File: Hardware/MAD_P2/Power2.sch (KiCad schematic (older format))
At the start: 91 parts, among them U13 XL1509-5.0, U14 XL1509-5.0, U15 AMS1117-3.3, U16 AMS1117-3.3, U18 AMS1117-3.3, U22 XL1509-5.0, U24 AMS1117-3.3

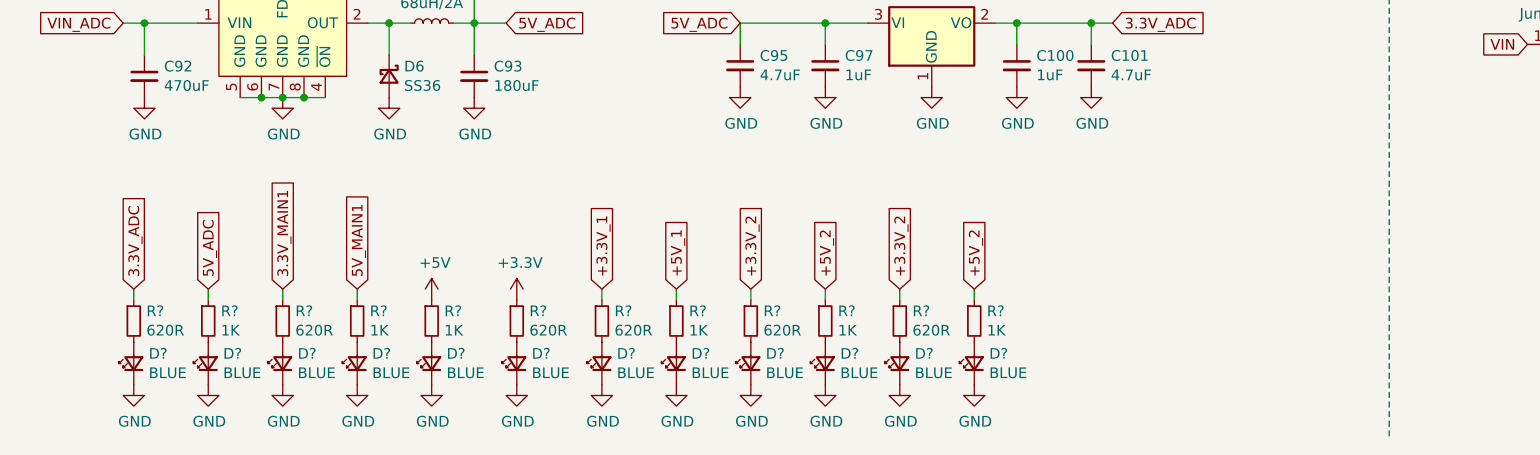
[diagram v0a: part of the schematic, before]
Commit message: added optional sd card socket for data
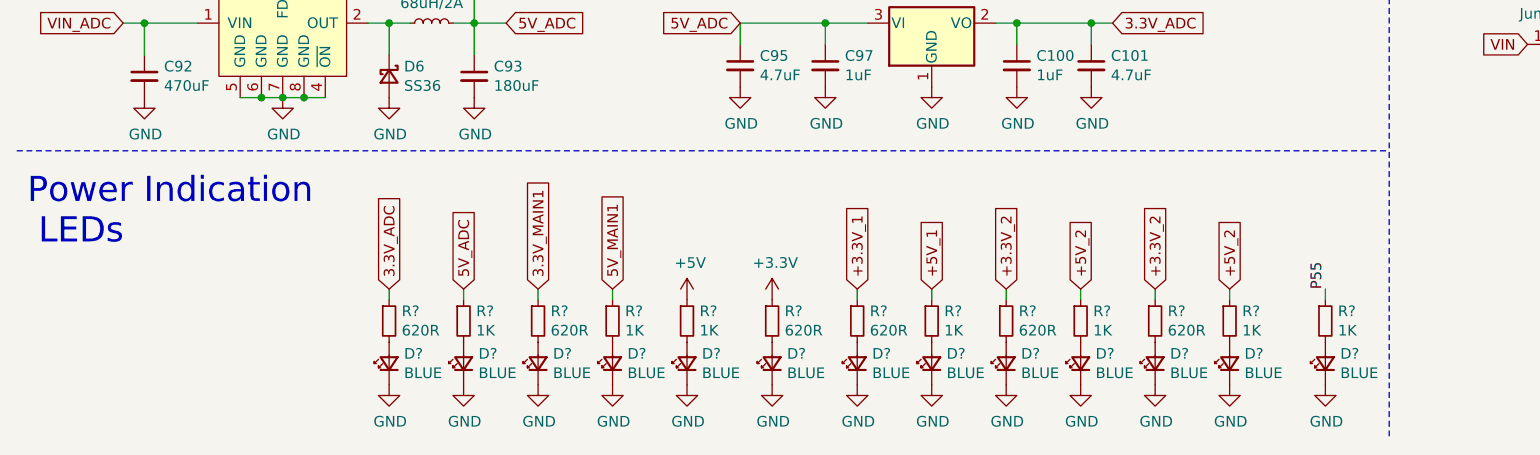
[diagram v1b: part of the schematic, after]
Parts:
- added D?: BLUE, symbol Device:LED_Small
- added R?: 1K, symbol Device:R_Small
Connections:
- net GND: now also D?.1 (K)
- new net: D?.2 (A), R?.2
- new net P55: R?.1
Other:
- note added: "Power Indication\n LEDs"
- moved on the sheet: D?, R?

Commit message: revising pcb layout
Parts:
- D13, D14, D15, D16, D17, D18, D19, D20, D21, D22, D5, D7, D8: renamed from D?; footprint (none) -> LED_SMD:LED_0603_1608Metric
- J1, J12, J17, J2, J27, J28, J29, J3, J30: renamed from J?; footprint Connector_AMASS:AMASS_XT30PW-M_1x02_P2.50mm_Horizontal -> MAD_P2:0705530001
- JP1, JP11, JP12, JP2, JP21, JP22, JP23, JP24, JP25, JP26, JP27, JP28, JP29, JP3, JP30, JP31, JP32, JP33, JP34, JP35, JP36, JP4, JP5, JP6, JP7, JP8, JP9: renamed from JP?; footprint Connector_PinHeader_2.54mm:PinHeader_1x02_P2.54mm_Vertical -> Jumper:SolderJumper-2_P1.3mm_Open_Pad1.0x1.5mm
- R12, R13, R25, R3, R30, R31, R32, R33, R34, R4, R5, R7, R8: renamed from R?; footprint (none) -> Resistor_SMD:R_0603_1608Metric
- gave numbers to parts that had none: 2

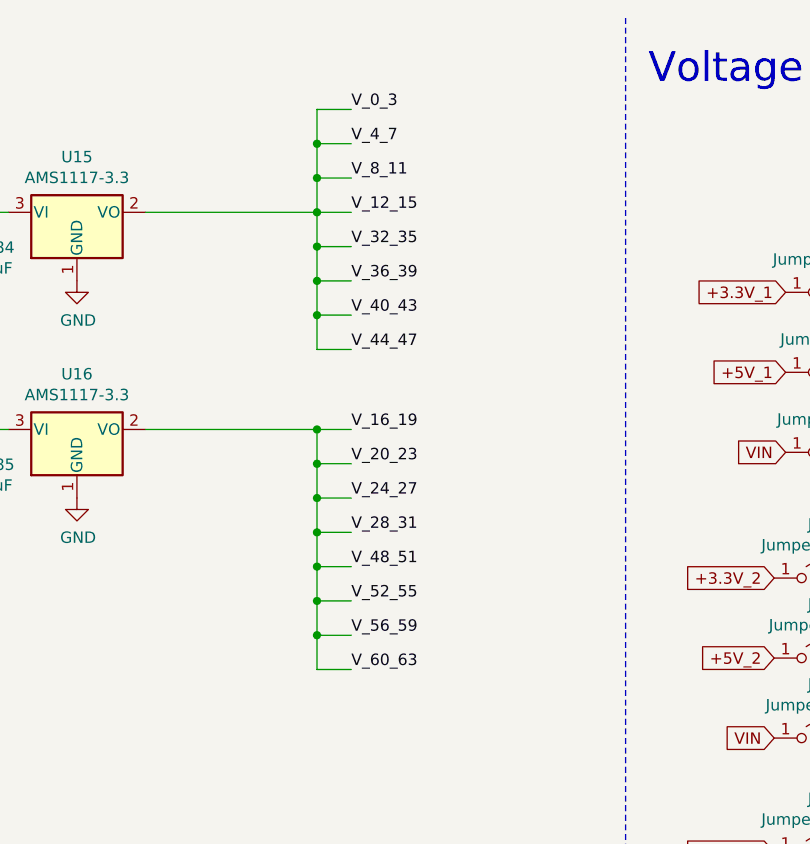
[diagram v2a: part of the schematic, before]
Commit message: routed adc
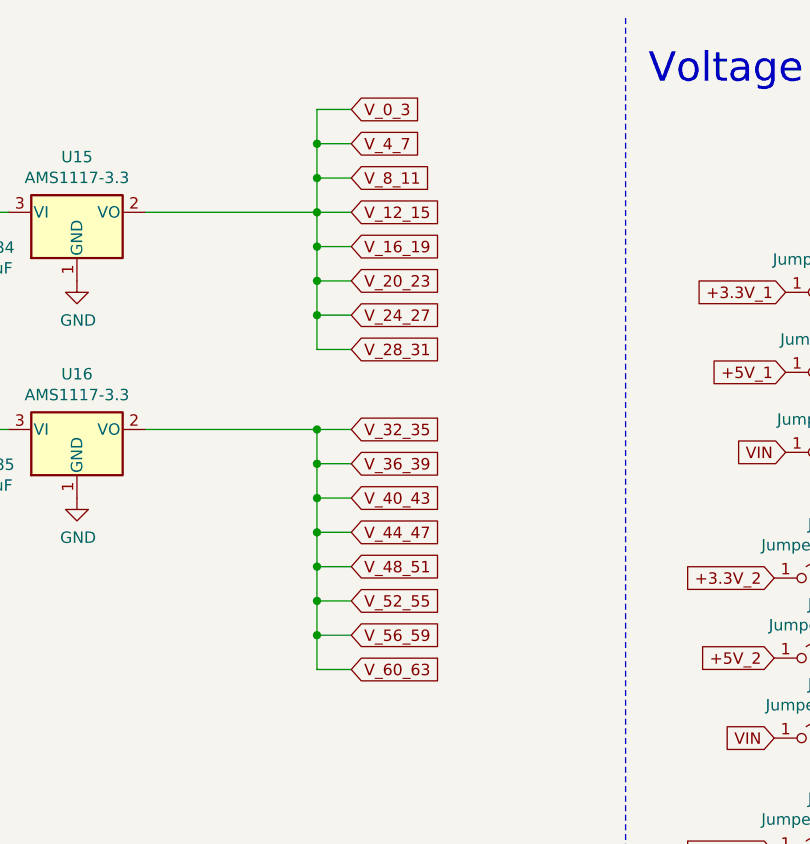
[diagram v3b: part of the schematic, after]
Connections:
- net V_16_19 renamed V_32_35
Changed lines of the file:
@@
 	3600 2300 4050 2300
-Wire Wire Line
-	5600 2750 5600 2600
-Wire Wire Line
-	5600 2750 5750 2750
-Connection ~ 5600 2750
-Wire Wire Line
-	5600 2600 5750 2600
-Wire Wire Line
-	5600 2600 5600 2450
-Wire Wire Line
-	5600 2450 5750 2450
-Connection ~ 5600 2600
-Wire Wire Line
-	5600 2450 5600 2300
-Wire Wire Line
-	5600 2300 5750 2300
-Connection ~ 5600 2450
-Text Label 5750 2600 0    50   ~ 0
-V_24_27
-Text Label 5750 2750 0    50   ~ 0
-V_28_31
 Wire Wire Line
 	3250 1800 3250 2300
@@
 	5600 1500 5750 1500
 Connection ~ 5600 1650
-Wire Wire Line
-	5600 3350 5600 3200
-Wire Wire Line
-	5600 3350 5750 3350
-Wire Wire Line
-	5600 3200 5750 3200
-Wire Wire Line
-	5600 3200 5600 3050
-Wire Wire Line
-	5600 3050 5750 3050
-Connection ~ 5600 3200
-Wire Wire Line
-	5600 3050 5600 2900
-Wire Wire Line
-	5600 2900 5750 2900
-Connection ~ 5600 3050
-Text Label 5750 2450 0    50   ~ 0
-V_20_23
-Text Label 5750 2300 0    50   ~ 0
-V_16_19
-Text Label 5750 1350 0    50   ~ 0
-V_12_15
-Text Label 5750 1200 0    50   ~ 0
-V_8_11
-Text Label 5750 1050 0    50   ~ 0
-V_4_7
-Text Label 5750 900  0    50   ~ 0
-V_0_3
-Text Label 5750 1500 0    50   ~ 0
-V_32_35
-Text Label 5750 1650 0    50   ~ 0
-V_36_39
-Text Label 5750 1800 0    50   ~ 0
-V_40_43
-Text Label 5750 1950 0    50   ~ 0
-V_44_47
-Text Label 5750 2900 0    50   ~ 0
-V_48_51
-Text Label 5750 3050 0    50   ~ 0
-V_52_55
-Text Label 5750 3200 0    50   ~ 0
-V_56_59
-Text Label 5750 3350 0    50   ~ 0
-V_60_63
 Wire Wire Line
 	4850 1350 5600 1350
@@
 	6950 500  6950 7800
 Wire Wire Line
-	5600 2900 5600 2750
-Connection ~ 5600 2900
-Wire Wire Line
 	5600 1500 5600 1350
 Connection ~ 5600 1500
 Wire Wire Line
 	4850 2300 5600 2300
-Connection ~ 5600 2300
 Text GLabel 1100 3950 0    50   Input ~ 0
 VIN_MAIN
@@
 Wire Notes Line
 	500  6450 6950 6450
+Text GLabel 5750 900  2    50   Input ~ 0
+V_0_3
+Text GLabel 5750 1050 2    50   Input ~ 0
+V_4_7
+Text GLabel 5750 1200 2    50   Input ~ 0
+V_8_11
+Text GLabel 5750 1350 2    50   Input ~ 0
+V_12_15
+Text GLabel 5750 1650 2    50   Input ~ 0
+V_20_23
+Text GLabel 5750 1500 2    50   Input ~ 0
+V_16_19
+Text GLabel 5750 1800 2    50   Input ~ 0
+V_24_27
+Text GLabel 5750 1950 2    50   Input ~ 0
+V_28_31
+Text GLabel 5750 3350 2    50   Input ~ 0
+V_60_63
+Text GLabel 5750 3200 2    50   Input ~ 0
+V_56_59
+Text GLabel 5750 3050 2    50   Input ~ 0
+V_52_55
+Text GLabel 5750 2900 2    50   Input ~ 0
+V_48_51
+Text GLabel 5750 2750 2    50   Input ~ 0
+V_44_47
+Text GLabel 5750 2600 2    50   Input ~ 0
+V_40_43
+Text GLabel 5750 2450 2    50   Input ~ 0
+V_36_39
+Text GLabel 5750 2300 2    50   Input ~ 0
+V_32_35
+Connection ~ 5600 2900
+Wire Wire Line
+	5600 2900 5750 2900
+Wire Wire Line
+	5600 3050 5600 2900
+Connection ~ 5600 3050
+Wire Wire Line
+	5600 3050 5750 3050
+Wire Wire Line
+	5600 3200 5600 3050
+Wire Wire Line
+	5600 3350 5600 3200
+Connection ~ 5600 3200
+Wire Wire Line
+	5600 3200 5750 3200
+Wire Wire Line
+	5600 3350 5750 3350
+Connection ~ 5600 2300
+Wire Wire Line
+	5600 2300 5750 2300
+Wire Wire Line
+	5600 2450 5600 2300
+Connection ~ 5600 2450
+Wire Wire Line
+	5600 2450 5750 2450
+Wire Wire Line
+	5600 2600 5600 2450
+Connection ~ 5600 2600
+Wire Wire Line
+	5600 2600 5750 2600
+Wire Wire Line
+	5600 2900 5600 2750
+Wire Wire Line
+	5600 2750 5600 2600
+Connection ~ 5600 2750
+Wire Wire Line
+	5600 2750 5750 2750
 $EndSCHEMATC

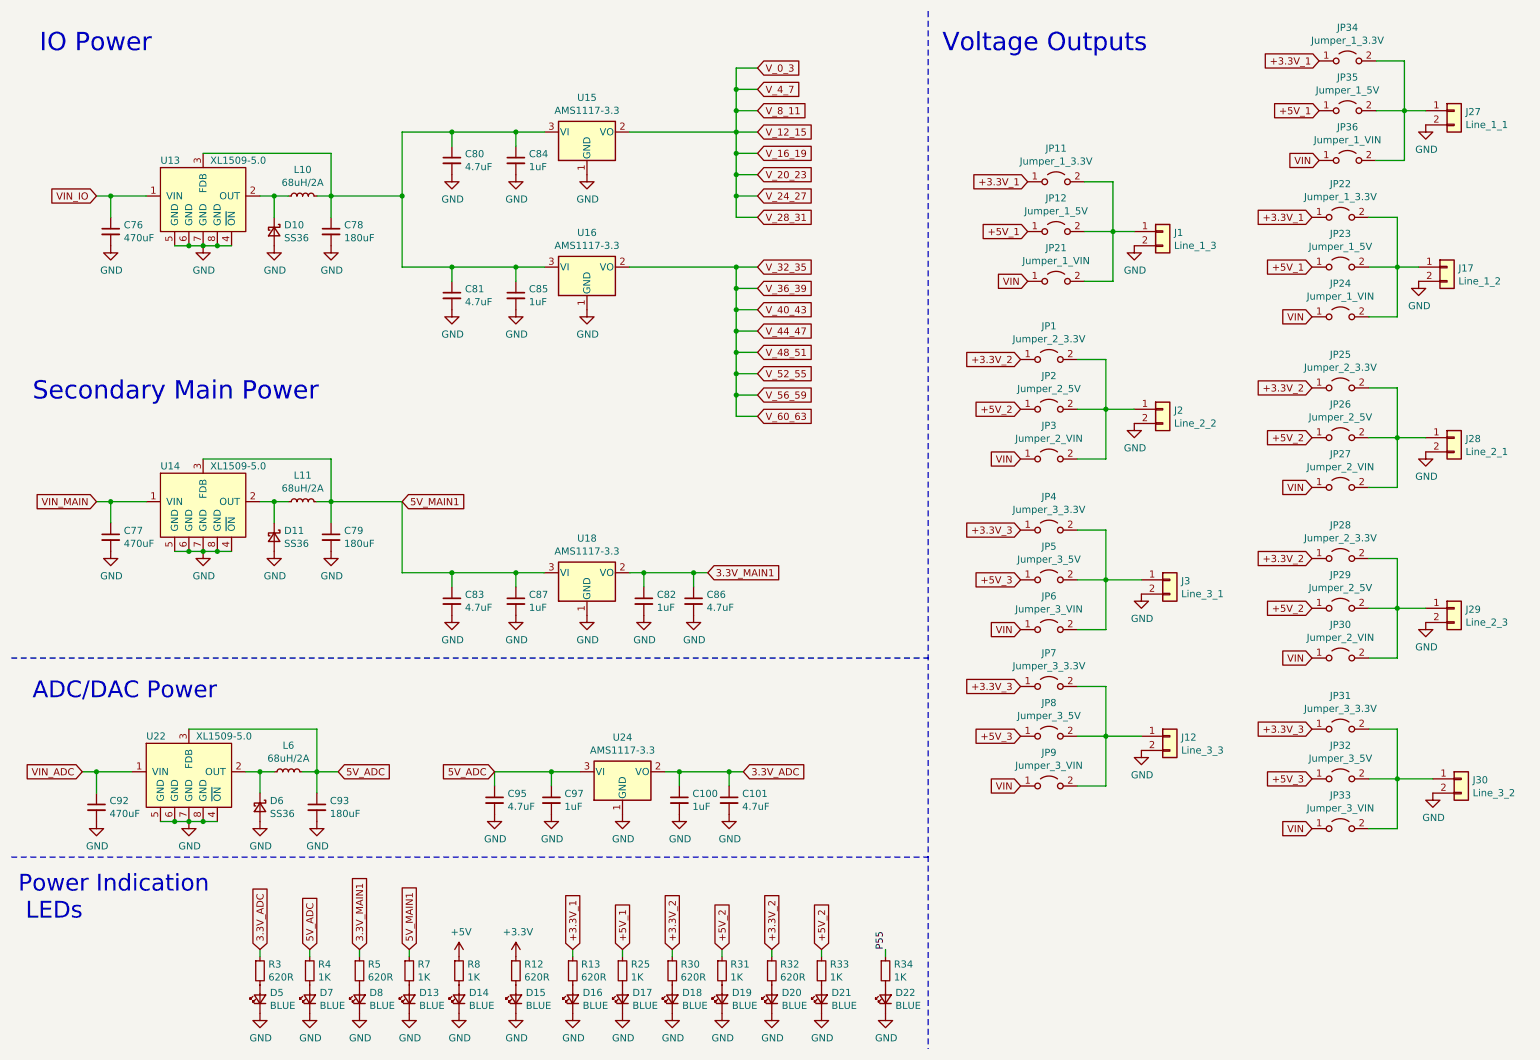
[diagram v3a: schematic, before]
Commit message: changed to 4 layer board due to number of wires to route. Routed ground and power nets
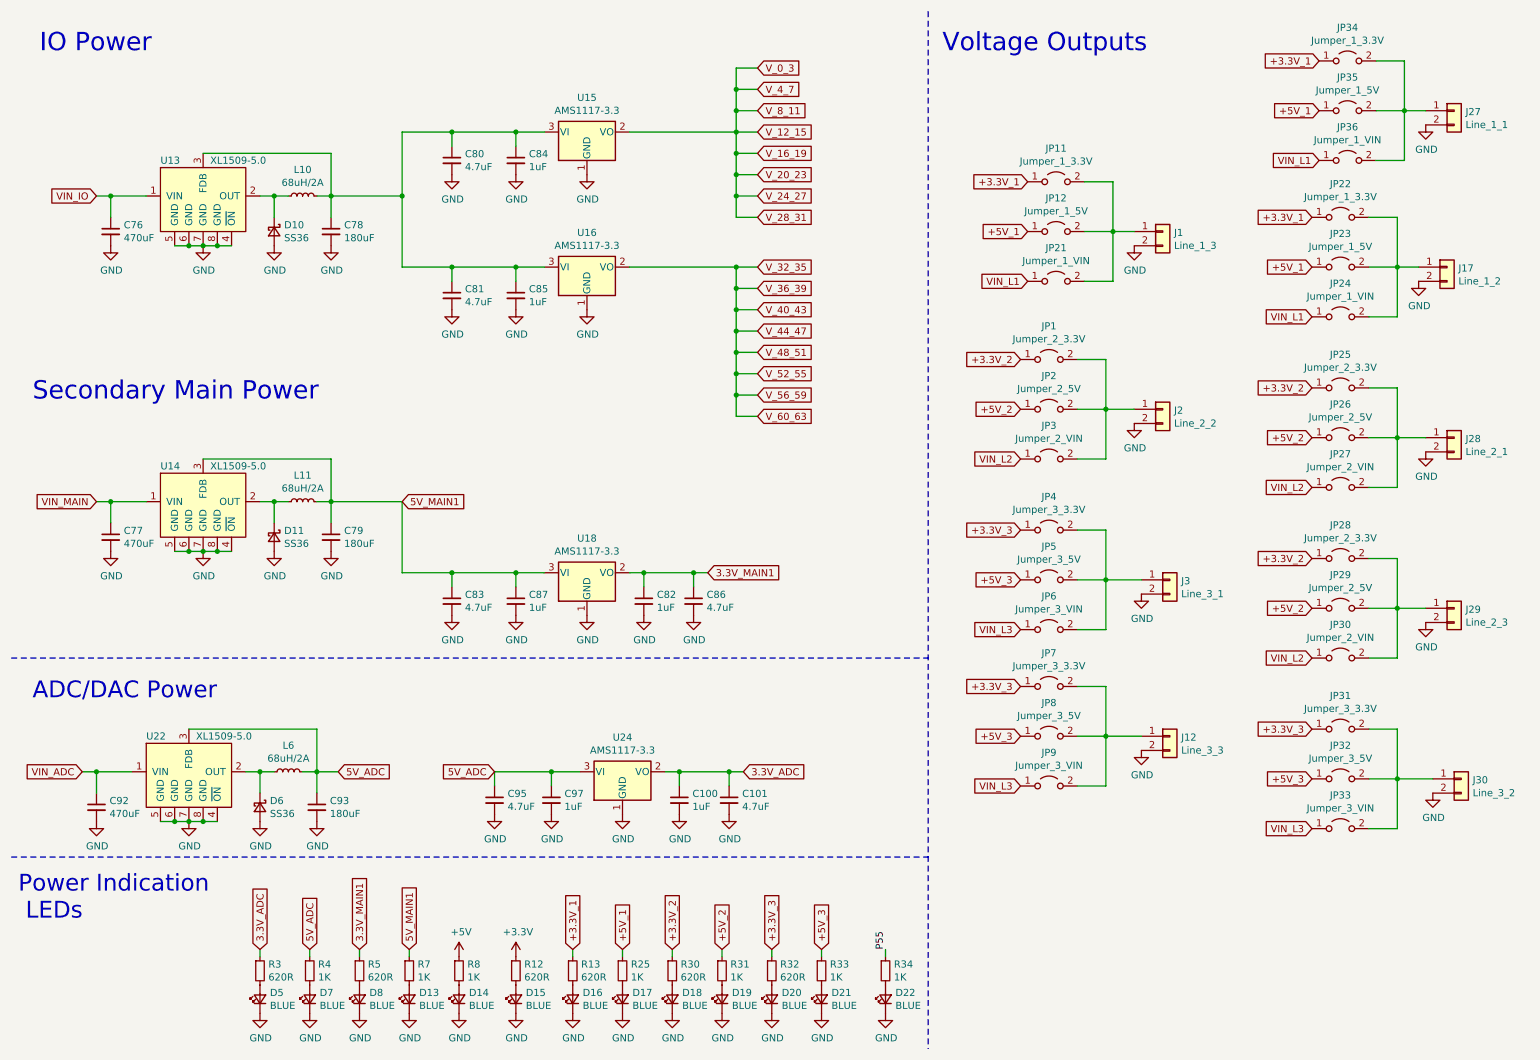
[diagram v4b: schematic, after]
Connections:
- net +3.3V_2: no longer R32.1
- net +3.3V_3: now also R32.1
- net +5V_2: no longer R33.1
- net +5V_3: now also R33.1
- removed net VIN: JP21.1 (A), JP24.1 (A), JP27.1 (A), JP3.1 (A), JP30.1 (A), JP33.1 (A), JP36.1 (A), JP6.1 (A), JP9.1 (A)
- new net VIN_L1: JP21.1 (A), JP24.1 (A), JP36.1 (A)
- new net VIN_L2: JP27.1 (A), JP3.1 (A), JP30.1 (A)
- new net VIN_L3: JP33.1 (A), JP6.1 (A), JP9.1 (A)
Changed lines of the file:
@@
 $EndComp
 Text GLabel 9700 1550 0    50   Input ~ 0
-VIN
+VIN_L1
 $Comp
 L Connector_Generic:Conn_01x02 J?
@@
 $EndComp
 Text GLabel 9650 3850 0    50   Input ~ 0
-VIN
+VIN_L2
 $Comp
 L Connector_Generic:Conn_01x02 J?
@@
 $EndComp
 Text GLabel 7600 4850 0    50   Input ~ 0
-VIN
+VIN_L3
 $Comp
 L Connector_Generic:Conn_01x02 J?
@@
 $EndComp
 Text GLabel 9650 2650 0    50   Input ~ 0
-VIN
+VIN_L1
 $Comp
 L Connector_Generic:Conn_01x02 J?
@@
 $EndComp
 Text GLabel 7650 2400 0    50   Input ~ 0
-VIN
+VIN_L1
 $Comp
 L Connector_Generic:Conn_01x02 J?
@@
 $EndComp
 Text GLabel 7600 3650 0    50   Input ~ 0
-VIN
+VIN_L2
 $Comp
 L Connector_Generic:Conn_01x02 J?
@@
 $EndComp
 Text GLabel 9650 5050 0    50   Input ~ 0
-VIN
+VIN_L2
 $Comp
 L Connector_Generic:Conn_01x02 J?
@@
 $EndComp
 Text GLabel 9650 6250 0    50   Input ~ 0
-VIN
+VIN_L3
 $Comp
 L Connector_Generic:Conn_01x02 J?
@@
 $EndComp
 Text GLabel 7600 5950 0    50   Input ~ 0
-VIN
+VIN_L3
 $Comp
 L Connector_Generic:Conn_01x02 J?
@@
 +5V_2
 Text GLabel 5850 7100 1    50   Input ~ 0
-+3.3V_2
++3.3V_3
 $Comp
 L Device:LED_Small D?
@@
 $EndComp
 Text GLabel 6200 7100 1    50   Input ~ 0
-+5V_2
++5V_3
 Wire Wire Line
 	6650 7100 6650 7150

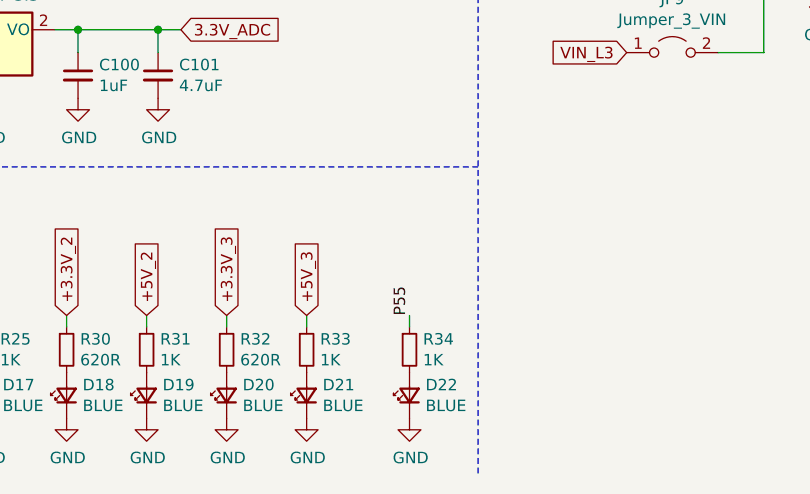
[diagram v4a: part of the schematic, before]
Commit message: fixed DAC issue and added silkscreen
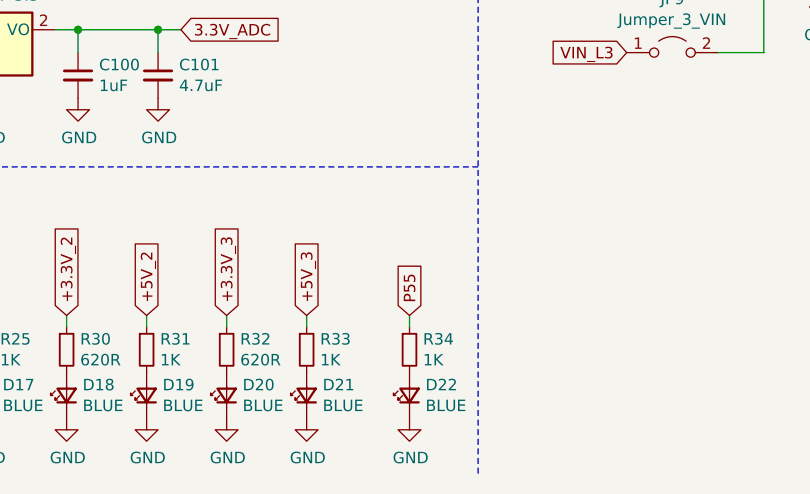
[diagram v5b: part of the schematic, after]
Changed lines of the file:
@@
 	0    -1   -1   0
 $EndComp
-Text Label 6650 7100 1    50   ~ 0
-P55
 Text Notes 550  6900 0    118  ~ 0
 Power Indication\n LEDs
@@
 Wire Wire Line
 	5600 2750 5750 2750
+Text GLabel 6650 7100 1    50   Input ~ 0
+P55
 $EndSCHEMATC

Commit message: completed BOM with digikey and LSCS parts
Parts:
- C100, C82, C84, C85, C87, C97: LCSC (none) -> C15849; TYPE (none) -> BASIC
- C101, C80, C81, C83, C86, C95: LCSC (none) -> C19666; TYPE (none) -> BASIC
- C76, C77, C92: DIGIKEY (none) -> 399-18277-1-ND; LCSC (none) -> C3350; TYPE (none) -> EXT
- C78, C79, C93: DIGIKEY (none) -> 1189-2158-ND; LCSC (none) -> C413657; TYPE (none) -> EXT
- D10, D11, D6: LCSC (none) -> C35722; TYPE (none) -> BASIC
- D13, D14, D15, D16, D17, D18, D19, D20, D21, D22, D5, D7, D8: LCSC (none) -> C72041; TYPE (none) -> BASIC
- J1, J12, J17, J2, J27, J28, J29, J3, J30: DIGIKEY (none) -> WM4900-ND; TYPE (none) -> DIGIKEY
- JP1, JP11, JP12, JP2, JP21, JP22, JP23, JP24, JP25, JP26, JP27, JP28, JP29, JP3, JP30, JP31, JP32, JP33, JP34, JP35, JP36, JP4, JP5, JP6, JP7, JP8, JP9: TYPE (none) -> NA
- L10, L11, L6: LCSC (none) -> C497902; TYPE (none) -> EXT
- R12, R13, R3, R30, R32, R5: LCSC (none) -> C23220; TYPE (none) -> BASIC
- R25, R31, R33, R34, R4, R7, R8: LCSC (none) -> C21190; TYPE (none) -> BASIC
- U13, U14, U22: LCSC (none) -> C61063; TYPE (none) -> BASIC
- U15, U16, U18, U24: LCSC (none) -> C6186; TYPE (none) -> BASIC
